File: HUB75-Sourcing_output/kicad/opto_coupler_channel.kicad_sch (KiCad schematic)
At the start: 4 parts, among them U16 LTV-827

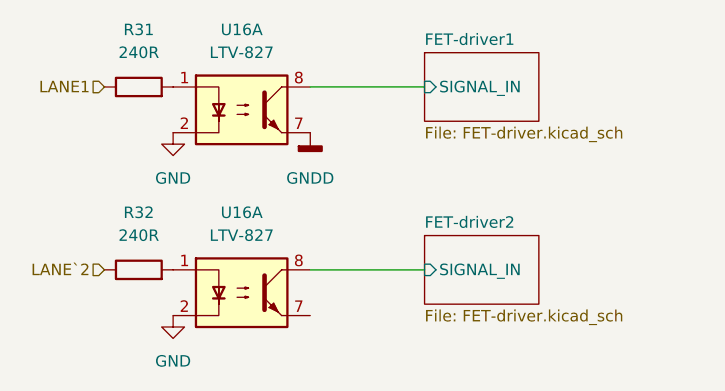
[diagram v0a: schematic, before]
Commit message: Update board with current mirror + backup
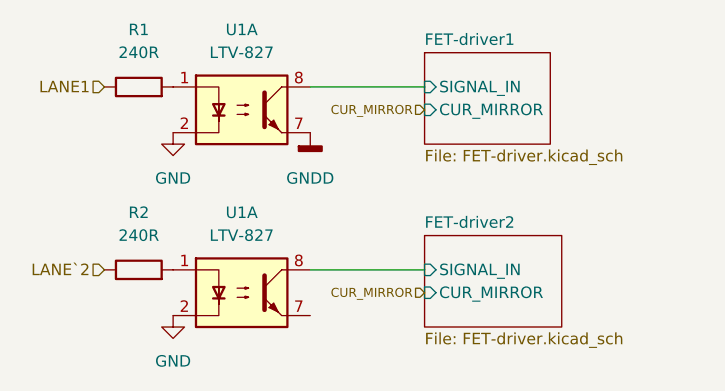
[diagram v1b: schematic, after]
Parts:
- R1: renamed from R31; footprint Resistor_SMD:R_2010_5025Metric_Pad1.40x2.65mm_HandSolder -> Resistor_SMD:R_1206_3216Metric_Pad1.30x1.75mm_HandSolder
- R2: renamed from R32; footprint Resistor_SMD:R_2010_5025Metric_Pad1.40x2.65mm_HandSolder -> Resistor_SMD:R_1206_3216Metric_Pad1.30x1.75mm_HandSolder
- renumbered U16 to U1
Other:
- sheet FET-driver1 ports: added CUR_MIRROR; removed none
- sheet FET-driver2 ports: added CUR_MIRROR; removed none
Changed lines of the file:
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@@
     (effects (font (size 1.27 1.27)) (justify right))
+  )
+  (hierarchical_label "CUR_MIRROR" (shape input) (at 77.47 55.88 180)
+    (effects (font (size 1 1)) (justify right))
+  )
+  (hierarchical_label "CUR_MIRROR" (shape input) (at 77.47 35.56 180)
+    (effects (font (size 1 1)) (justify right))
   )
   (hierarchical_label "LANE1" (shape input) (at 41.91 33.02 180)
@@
   (symbol (lib_id "power:GND") (at 49.53 38.1 0)
     (in_bom yes) (on_board yes) (fields_autoplaced)
-    (property "Reference" "#PWR036" (id 0) (at 49.53 44.45 0)
+    (property "Reference" "#PWR01" (id 0) (at 49.53 44.45 0)
       (effects (font (size 1.27 1.27)) hide)
     )
@@
   (symbol (lib_id "Device:R") (at 45.72 53.34 90)
     (in_bom yes) (on_board yes) (fields_autoplaced)
-    (property "Reference" "R32" (id 0) (at 45.72 46.99 90))
+    (property "Reference" "R2" (id 0) (at 45.72 46.99 90))
     (property "Value" "240R" (id 1) (at 45.72 49.53 90))
-    (property "Footprint" "Resistor_SMD:R_2010_5025Metric_Pad1.40x2.65mm_HandSolder" (id 2) (at 45.72 55.118 90)
+    (property "Footprint" "Resistor_SMD:R_1206_3216Metric_Pad1.30x1.75mm_HandSolder" (id 2) (at 45.72 55.118 90)
       (effects (font (size 1.27 1.27)) hide)
     )
@@
   (symbol (lib_id "power:GND") (at 49.53 58.42 0)
     (in_bom yes) (on_board yes) (fields_autoplaced)
-    (property "Reference" "#PWR037" (id 0) (at 49.53 64.77 0)
+    (property "Reference" "#PWR02" (id 0) (at 49.53 64.77 0)
       (effects (font (size 1.27 1.27)) hide)
     )
@@
   (symbol (lib_id "Device:R") (at 45.72 33.02 90)
     (in_bom yes) (on_board yes) (fields_autoplaced)
-    (property "Reference" "R31" (id 0) (at 45.72 26.67 90))
+    (property "Reference" "R1" (id 0) (at 45.72 26.67 90))
     (property "Value" "240R" (id 1) (at 45.72 29.21 90))
-    (property "Footprint" "Resistor_SMD:R_2010_5025Metric_Pad1.40x2.65mm_HandSolder" (id 2) (at 45.72 34.798 90)
+    (property "Footprint" "Resistor_SMD:R_1206_3216Metric_Pad1.30x1.75mm_HandSolder" (id 2) (at 45.72 34.798 90)
       (effects (font (size 1.27 1.27)) hide)
     )
@@
   (symbol (lib_id "Isolator:LTV-827") (at 57.15 55.88 0)
     (in_bom yes) (on_board yes) (fields_autoplaced)
-    (property "Reference" "U16" (id 0) (at 57.15 46.99 0))
+    (property "Reference" "U1" (id 0) (at 57.15 46.99 0))
     (property "Value" "LTV-827" (id 1) (at 57.15 49.53 0))
     (property "Footprint" "Package_DIP:DIP-8_W7.62mm" (id 2) (at 52.07 60.96 0)
@@
   (symbol (lib_id "Isolator:LTV-827") (at 57.15 35.56 0)
     (in_bom yes) (on_board yes) (fields_autoplaced)
-    (property "Reference" "U16" (id 0) (at 57.15 26.67 0))
+    (property "Reference" "U1" (id 0) (at 57.15 26.67 0))
     (property "Value" "LTV-827" (id 1) (at 57.15 29.21 0))
     (property "Footprint" "Package_DIP:DIP-8_W7.62mm" (id 2) (at 52.07 40.64 0)
@@
   (symbol (lib_id "power:GNDD") (at 64.77 38.1 0)
     (in_bom yes) (on_board yes) (fields_autoplaced)
-    (property "Reference" "#PWR038" (id 0) (at 64.77 44.45 0)
+    (property "Reference" "#PWR03" (id 0) (at 64.77 44.45 0)
       (effects (font (size 1.27 1.27)) hide)
     )
@@
     (pin "1")
   )
-  (sheet (at 77.47 49.53) (size 12.7 7.62) (fields_autoplaced)
+  (sheet (at 77.47 49.53) (size 15.24 10.16) (fields_autoplaced)
     (stroke (width 0.1524) (type solid) (color 0 0 0 0))
     (fill (color 0 0 0 0.0000))
@@
       (effects (font (size 1.27 1.27)) (justify left bottom))
     )
-    (property "Sheet file" "FET-driver.kicad_sch" (id 1) (at 77.47 57.7346 0)
+    (property "Sheet file" "FET-driver.kicad_sch" (id 1) (at 77.47 60.2746 0)
       (effects (font (size 1.27 1.27)) (justify left top))
     )
@@
       (effects (font (size 1.27 1.27)) (justify left))
     )
+    (pin "CUR_MIRROR" input (at 77.47 55.88 180)
+      (effects (font (size 1.27 1.27)) (justify left))
+    )
   )
-  (sheet (at 77.47 29.21) (size 12.7 7.62) (fields_autoplaced)
+  (sheet (at 77.47 29.21) (size 13.97 10.16) (fields_autoplaced)
     (stroke (width 0.1524) (type solid) (color 0 0 0 0))
     (fill (color 0 0 0 0.0000))
@@
       (effects (font (size 1.27 1.27)) (justify left bottom))
     )
-    (property "Sheet file" "FET-driver.kicad_sch" (id 1) (at 77.47 37.4146 0)
+    (property "Sheet file" "FET-driver.kicad_sch" (id 1) (at 77.47 39.9546 0)
       (effects (font (size 1.27 1.27)) (justify left top))
     )
@@
       (effects (font (size 1.27 1.27)) (justify left))
     )
+    (pin "CUR_MIRROR" input (at 77.47 35.56 180)
+      (effects (font (size 1.27 1.27)) (justify left))
+    )

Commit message: Update label
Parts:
- renumbered R1 to R31, R2 to R32, U1 to U16
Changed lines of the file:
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@@
   (symbol (lib_id "power:GND") (at 49.53 38.1 0)
     (in_bom yes) (on_board yes) (fields_autoplaced)
-    (property "Reference" "#PWR01" (id 0) (at 49.53 44.45 0)
+    (property "Reference" "#PWR036" (id 0) (at 49.53 44.45 0)
       (effects (font (size 1.27 1.27)) hide)
     )
@@
   (symbol (lib_id "Device:R") (at 45.72 53.34 90)
     (in_bom yes) (on_board yes) (fields_autoplaced)
-    (property "Reference" "R2" (id 0) (at 45.72 46.99 90))
+    (property "Reference" "R32" (id 0) (at 45.72 46.99 90))
     (property "Value" "240R" (id 1) (at 45.72 49.53 90))
     (property "Footprint" "Resistor_SMD:R_1206_3216Metric_Pad1.30x1.75mm_HandSolder" (id 2) (at 45.72 55.118 90)
@@
   (symbol (lib_id "power:GND") (at 49.53 58.42 0)
     (in_bom yes) (on_board yes) (fields_autoplaced)
-    (property "Reference" "#PWR02" (id 0) (at 49.53 64.77 0)
+    (property "Reference" "#PWR037" (id 0) (at 49.53 64.77 0)
       (effects (font (size 1.27 1.27)) hide)
     )
@@
   (symbol (lib_id "Device:R") (at 45.72 33.02 90)
     (in_bom yes) (on_board yes) (fields_autoplaced)
-    (property "Reference" "R1" (id 0) (at 45.72 26.67 90))
+    (property "Reference" "R31" (id 0) (at 45.72 26.67 90))
     (property "Value" "240R" (id 1) (at 45.72 29.21 90))
     (property "Footprint" "Resistor_SMD:R_1206_3216Metric_Pad1.30x1.75mm_HandSolder" (id 2) (at 45.72 34.798 90)
@@
   (symbol (lib_id "Isolator:LTV-827") (at 57.15 55.88 0)
     (in_bom yes) (on_board yes) (fields_autoplaced)
-    (property "Reference" "U1" (id 0) (at 57.15 46.99 0))
+    (property "Reference" "U16" (id 0) (at 57.15 46.99 0))
     (property "Value" "LTV-827" (id 1) (at 57.15 49.53 0))
     (property "Footprint" "Package_DIP:DIP-8_W7.62mm" (id 2) (at 52.07 60.96 0)
@@
   (symbol (lib_id "Isolator:LTV-827") (at 57.15 35.56 0)
     (in_bom yes) (on_board yes) (fields_autoplaced)
-    (property "Reference" "U1" (id 0) (at 57.15 26.67 0))
+    (property "Reference" "U16" (id 0) (at 57.15 26.67 0))
     (property "Value" "LTV-827" (id 1) (at 57.15 29.21 0))
     (property "Footprint" "Package_DIP:DIP-8_W7.62mm" (id 2) (at 52.07 40.64 0)
@@
   (symbol (lib_id "power:GNDD") (at 64.77 38.1 0)
     (in_bom yes) (on_board yes) (fields_autoplaced)
-    (property "Reference" "#PWR03" (id 0) (at 64.77 44.45 0)
+    (property "Reference" "#PWR038" (id 0) (at 64.77 44.45 0)
       (effects (font (size 1.27 1.27)) hide)
     )

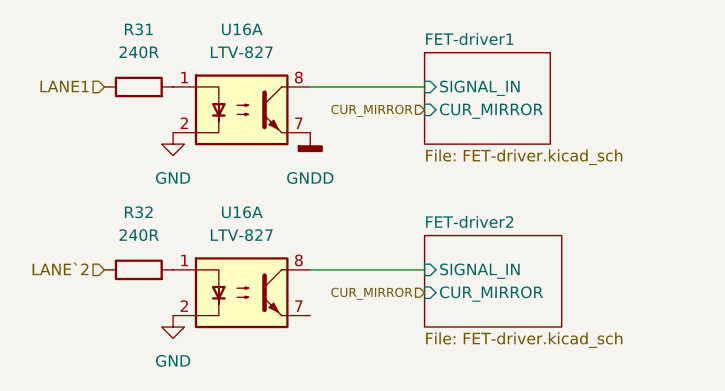
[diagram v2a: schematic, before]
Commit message: Remove incorrect GND connection
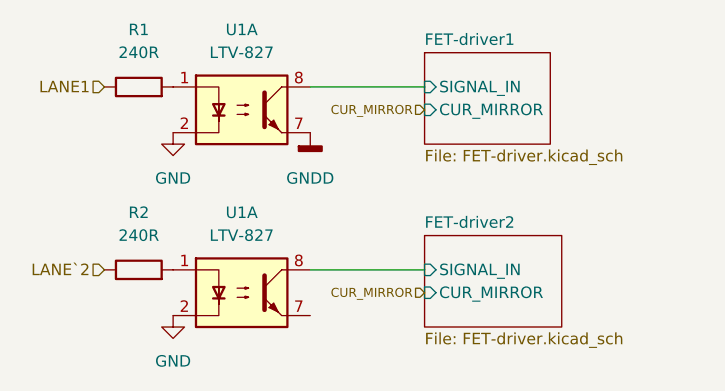
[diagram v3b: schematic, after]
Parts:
- renumbered R31 to R1, R32 to R2, U16 to U1
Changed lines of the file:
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@@
   (symbol (lib_id "power:GND") (at 49.53 38.1 0)
     (in_bom yes) (on_board yes) (fields_autoplaced)
-    (property "Reference" "#PWR036" (id 0) (at 49.53 44.45 0)
+    (property "Reference" "#PWR01" (id 0) (at 49.53 44.45 0)
       (effects (font (size 1.27 1.27)) hide)
     )
@@
   (symbol (lib_id "Device:R") (at 45.72 53.34 90)
     (in_bom yes) (on_board yes) (fields_autoplaced)
-    (property "Reference" "R32" (id 0) (at 45.72 46.99 90))
+    (property "Reference" "R2" (id 0) (at 45.72 46.99 90))
     (property "Value" "240R" (id 1) (at 45.72 49.53 90))
     (property "Footprint" "Resistor_SMD:R_1206_3216Metric_Pad1.30x1.75mm_HandSolder" (id 2) (at 45.72 55.118 90)
@@
   (symbol (lib_id "power:GND") (at 49.53 58.42 0)
     (in_bom yes) (on_board yes) (fields_autoplaced)
-    (property "Reference" "#PWR037" (id 0) (at 49.53 64.77 0)
+    (property "Reference" "#PWR02" (id 0) (at 49.53 64.77 0)
       (effects (font (size 1.27 1.27)) hide)
     )
@@
   (symbol (lib_id "Device:R") (at 45.72 33.02 90)
     (in_bom yes) (on_board yes) (fields_autoplaced)
-    (property "Reference" "R31" (id 0) (at 45.72 26.67 90))
+    (property "Reference" "R1" (id 0) (at 45.72 26.67 90))
     (property "Value" "240R" (id 1) (at 45.72 29.21 90))
     (property "Footprint" "Resistor_SMD:R_1206_3216Metric_Pad1.30x1.75mm_HandSolder" (id 2) (at 45.72 34.798 90)
@@
   (symbol (lib_id "Isolator:LTV-827") (at 57.15 55.88 0)
     (in_bom yes) (on_board yes) (fields_autoplaced)
-    (property "Reference" "U16" (id 0) (at 57.15 46.99 0))
+    (property "Reference" "U1" (id 0) (at 57.15 46.99 0))
     (property "Value" "LTV-827" (id 1) (at 57.15 49.53 0))
     (property "Footprint" "Package_DIP:DIP-8_W7.62mm" (id 2) (at 52.07 60.96 0)
@@
   (symbol (lib_id "Isolator:LTV-827") (at 57.15 35.56 0)
     (in_bom yes) (on_board yes) (fields_autoplaced)
-    (property "Reference" "U16" (id 0) (at 57.15 26.67 0))
+    (property "Reference" "U1" (id 0) (at 57.15 26.67 0))
     (property "Value" "LTV-827" (id 1) (at 57.15 29.21 0))
     (property "Footprint" "Package_DIP:DIP-8_W7.62mm" (id 2) (at 52.07 40.64 0)
@@
   (symbol (lib_id "power:GNDD") (at 64.77 38.1 0)
     (in_bom yes) (on_board yes) (fields_autoplaced)
-    (property "Reference" "#PWR038" (id 0) (at 64.77 44.45 0)
+    (property "Reference" "#PWR03" (id 0) (at 64.77 44.45 0)
       (effects (font (size 1.27 1.27)) hide)
     )

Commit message: New version after prototype failed
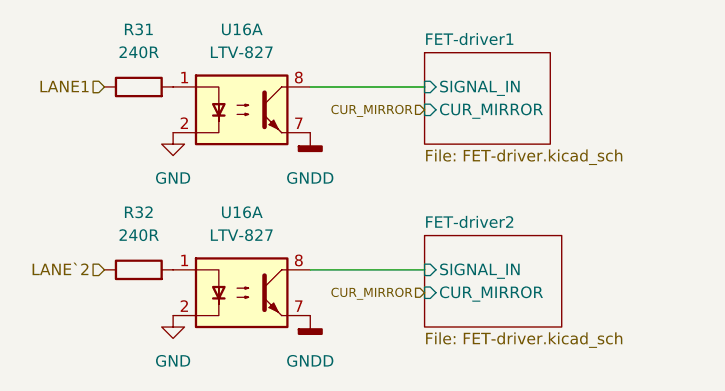
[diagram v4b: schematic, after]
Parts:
- renumbered R1 to R31, R2 to R32, U1 to U16
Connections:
- net GNDD: now also U16.7
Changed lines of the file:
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@@
   (symbol (lib_id "power:GND") (at 49.53 38.1 0)
     (in_bom yes) (on_board yes) (fields_autoplaced)
-    (property "Reference" "#PWR01" (id 0) (at 49.53 44.45 0)
+    (property "Reference" "#PWR036" (id 0) (at 49.53 44.45 0)
       (effects (font (size 1.27 1.27)) hide)
     )
@@
     (pin "1")
   )
+  (symbol (lib_id "power:GNDD") (at 64.77 58.42 0)
+    (in_bom yes) (on_board yes) (fields_autoplaced)
+    (property "Reference" "#PWR0110" (id 0) (at 64.77 64.77 0)
+      (effects (font (size 1.27 1.27)) hide)
+    )
+    (property "Value" "GNDD" (id 1) (at 64.77 63.5 0))
+    (property "Footprint" "" (id 2) (at 64.77 58.42 0)
+      (effects (font (size 1.27 1.27)) hide)
+    )
+    (property "Datasheet" "" (id 3) (at 64.77 58.42 0)
+      (effects (font (size 1.27 1.27)) hide)
+    )
+    (pin "1")
+  )
   (symbol (lib_id "Device:R") (at 45.72 53.34 90)
     (in_bom yes) (on_board yes) (fields_autoplaced)
-    (property "Reference" "R2" (id 0) (at 45.72 46.99 90))
+    (property "Reference" "R32" (id 0) (at 45.72 46.99 90))
     (property "Value" "240R" (id 1) (at 45.72 49.53 90))
     (property "Footprint" "Resistor_SMD:R_1206_3216Metric_Pad1.30x1.75mm_HandSolder" (id 2) (at 45.72 55.118 90)
@@
   (symbol (lib_id "power:GND") (at 49.53 58.42 0)
     (in_bom yes) (on_board yes) (fields_autoplaced)
-    (property "Reference" "#PWR02" (id 0) (at 49.53 64.77 0)
+    (property "Reference" "#PWR037" (id 0) (at 49.53 64.77 0)
       (effects (font (size 1.27 1.27)) hide)
     )
@@
   (symbol (lib_id "Device:R") (at 45.72 33.02 90)
     (in_bom yes) (on_board yes) (fields_autoplaced)
-    (property "Reference" "R1" (id 0) (at 45.72 26.67 90))
+    (property "Reference" "R31" (id 0) (at 45.72 26.67 90))
     (property "Value" "240R" (id 1) (at 45.72 29.21 90))
     (property "Footprint" "Resistor_SMD:R_1206_3216Metric_Pad1.30x1.75mm_HandSolder" (id 2) (at 45.72 34.798 90)
@@
   (symbol (lib_id "Isolator:LTV-827") (at 57.15 55.88 0)
     (in_bom yes) (on_board yes) (fields_autoplaced)
-    (property "Reference" "U1" (id 0) (at 57.15 46.99 0))
+    (property "Reference" "U16" (id 0) (at 57.15 46.99 0))
     (property "Value" "LTV-827" (id 1) (at 57.15 49.53 0))
     (property "Footprint" "Package_DIP:DIP-8_W7.62mm" (id 2) (at 52.07 60.96 0)
@@
   (symbol (lib_id "Isolator:LTV-827") (at 57.15 35.56 0)
     (in_bom yes) (on_board yes) (fields_autoplaced)
-    (property "Reference" "U1" (id 0) (at 57.15 26.67 0))
+    (property "Reference" "U16" (id 0) (at 57.15 26.67 0))
     (property "Value" "LTV-827" (id 1) (at 57.15 29.21 0))
     (property "Footprint" "Package_DIP:DIP-8_W7.62mm" (id 2) (at 52.07 40.64 0)
@@
   (symbol (lib_id "power:GNDD") (at 64.77 38.1 0)
     (in_bom yes) (on_board yes) (fields_autoplaced)
-    (property "Reference" "#PWR03" (id 0) (at 64.77 44.45 0)
+    (property "Reference" "#PWR038" (id 0) (at 64.77 44.45 0)
       (effects (font (size 1.27 1.27)) hide)
     )
